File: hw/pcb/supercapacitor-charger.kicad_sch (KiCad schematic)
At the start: 13 parts, among them U2 TPS61094

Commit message: fix: updated schematics to pcb revision d
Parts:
- JP1: PN (none) -> -
- TP3: PN (none) -> -; now left out of the parts list

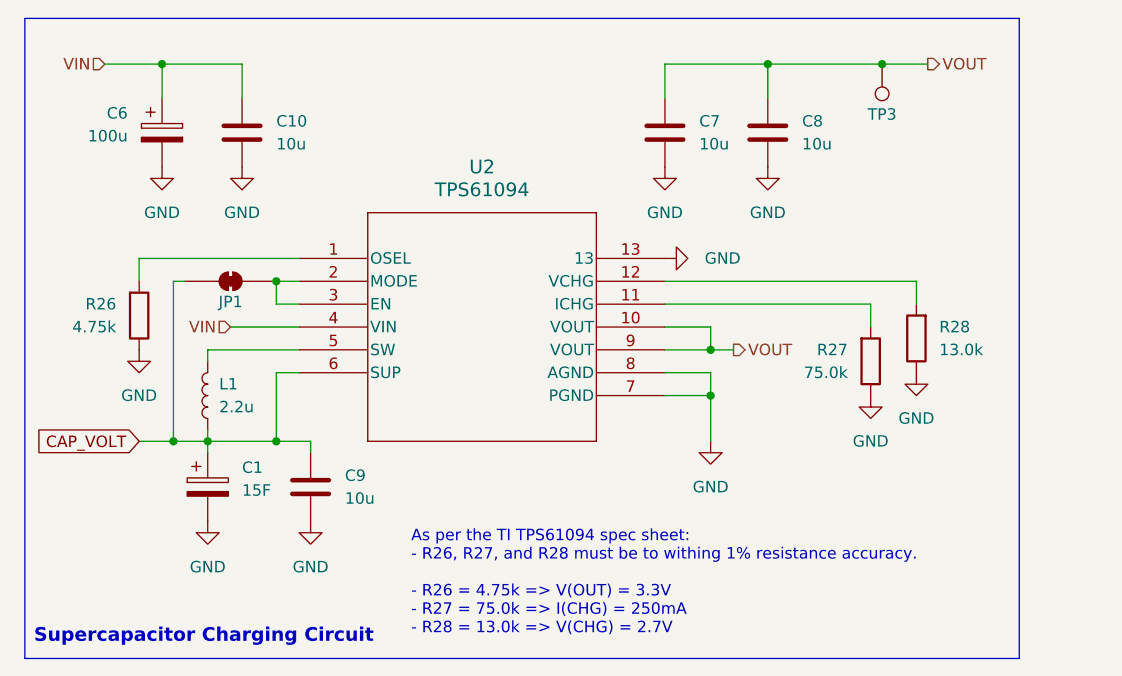
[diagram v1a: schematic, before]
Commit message: fix: added schottky diode or gate to enable pin
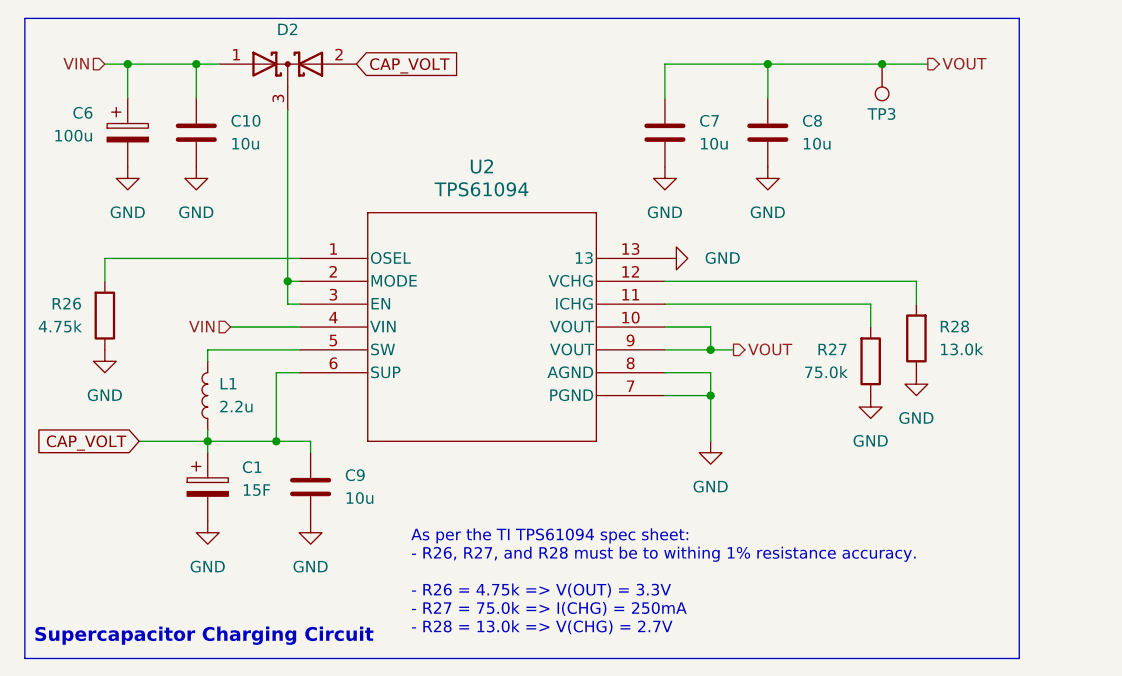
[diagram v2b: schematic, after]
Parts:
- removed JP1: SolderJumper_2_Bridged, Jumper:SolderJumper-2_P1.3mm_Bridged_RoundedPad1.0x1.5mm, symbol Jumper:SolderJumper_2_Bridged
- added D2: (no value), Package_TO_SOT_SMD:SOT-23, symbol Device:D_Schottky_Dual_CommonCathode_AAK
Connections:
- net CAP_VOLT: now also D2.2 (A)
- net VIN: now also D2.1 (A)
- net at U2.2 (MODE), U2.3 (EN): now also D2.3 (K)
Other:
- moved on the sheet: C10, C6, R26

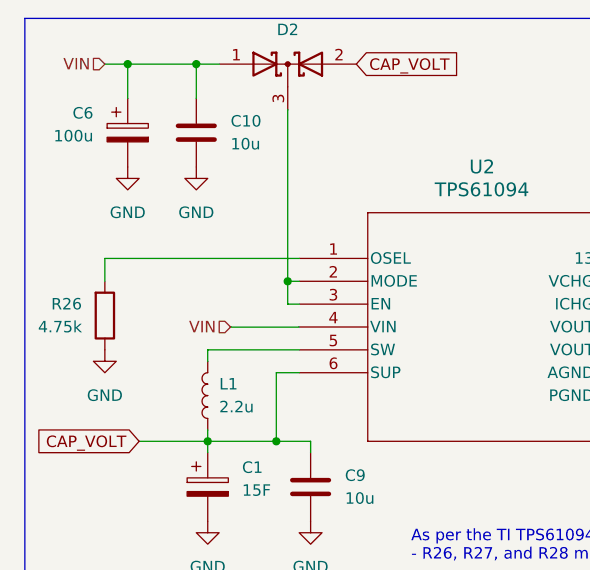
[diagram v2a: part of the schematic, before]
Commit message: fix: added or-ing diode to board
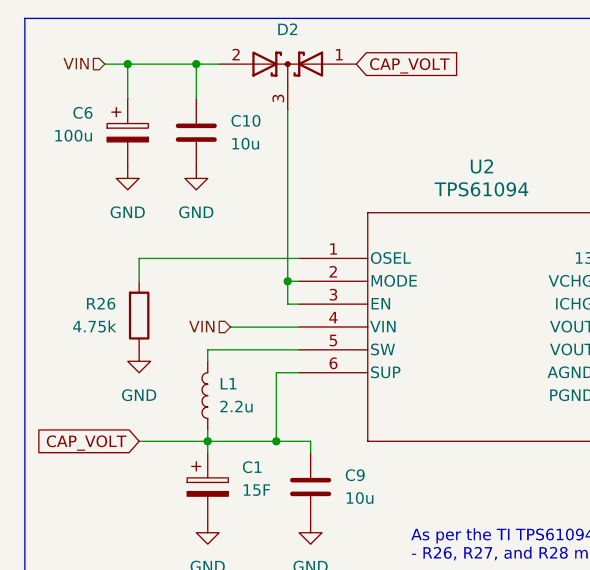
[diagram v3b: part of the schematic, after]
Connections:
- net CAP_VOLT: now also D2.1 (A); no longer D2.2 (A)
- net VIN: now also D2.2 (A); no longer D2.1 (A)
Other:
- moved on the sheet: R26
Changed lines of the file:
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@@
 	(wire
 		(pts
-			(xy 125.73 97.79) (xy 104.14 97.79)
+			(xy 125.73 97.79) (xy 107.95 97.79)
 		)
 		(stroke
@@
 	(wire
 		(pts
-			(xy 104.14 97.79) (xy 104.14 100.33)
+			(xy 107.95 97.79) (xy 107.95 100.33)
 		)
 		(stroke
@@
 	(symbol
 		(lib_id "power:GND")
-		(at 104.14 107.95 0)
+		(at 107.95 107.95 0)
 		(mirror y)
 		(unit 1)
@@
 		(fields_autoplaced yes)
 		(property "Reference" "#PWR034"
-			(at 104.14 114.3 0)
+			(at 107.95 114.3 0)
 			(hide yes)
 			(show_name no)
@@
 		)
 		(property "Value" "GND"
-			(at 104.14 113.03 0)
+			(at 107.95 113.03 0)
 			(show_name no)
 			(do_not_autoplace no)
@@
 		)
 		(property "Footprint" ""
-			(at 104.14 107.95 0)
+			(at 107.95 107.95 0)
 			(hide yes)
 			(show_name no)
@@
 		)
 		(property "Datasheet" ""
-			(at 104.14 107.95 0)
+			(at 107.95 107.95 0)
 			(hide yes)
 			(show_name no)
@@
 		)
 		(property "Description" "Power symbol creates a global label with name \"GND\" , ground"
-			(at 104.14 107.95 0)
+			(at 107.95 107.95 0)
 			(hide yes)
 			(show_name no)
@@
 	(symbol
 		(lib_id "Device:R")
-		(at 104.14 104.14 0)
+		(at 107.95 104.14 0)
 		(mirror x)
 		(unit 1)
@@
 		(fields_autoplaced yes)
 		(property "Reference" "R26"
-			(at 101.6 102.8699 0)
+			(at 105.41 102.8699 0)
 			(show_name no)
 			(do_not_autoplace no)
@@
 		)
 		(property "Value" "4.75k"
-			(at 101.6 105.4099 0)
+			(at 105.41 105.4099 0)
 			(show_name no)
 			(do_not_autoplace no)
@@
 		)
 		(property "Footprint" "Resistor_SMD:R_0603_1608Metric"
-			(at 102.362 104.14 90)
+			(at 106.172 104.14 90)
 			(hide yes)
 			(show_name no)
@@
 		)
 		(property "Datasheet" ""
-			(at 104.14 104.14 0)
+			(at 107.95 104.14 0)
 			(hide yes)
 			(show_name no)
@@
 		)
 		(property "Description" "Resistor"
-			(at 104.14 104.14 0)
+			(at 107.95 104.14 0)
 			(hide yes)
 			(show_name no)
@@
 		)
 		(property "PN" "CPF0603F4K75C1"
-			(at 104.14 104.14 0)
+			(at 107.95 104.14 0)
 			(hide yes)
 			(show_name no)
@@
 		)
 		(property "Field6" ""
-			(at 104.14 104.14 0)
+			(at 107.95 104.14 0)
 			(hide yes)
 			(show_name no)
@@
 		)
 		(property "Sim.Device" ""
-			(at 104.14 104.14 0)
+			(at 107.95 104.14 0)
 			(hide yes)
 			(show_name no)
@@
 		)
 		(property "Sim.Type" ""
-			(at 104.14 104.14 0)
+			(at 107.95 104.14 0)
 			(hide yes)
 			(show_name no)
@@
 		(lib_id "Device:D_Schottky_Dual_CommonCathode_AAK")
 		(at 124.46 76.2 0)
+		(mirror y)
 		(unit 1)
 		(body_style 1)
@@
 		(in_pos_files yes)
 		(dnp no)
-		(fields_autoplaced yes)
 		(property "Reference" "D2"
 			(at 124.46 72.39 0)

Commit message: chore: added stars to potentially different components
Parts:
- R28: value 13.0k -> 13.0k*
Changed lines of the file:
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@@
 			)
 		)
-		(property "Value" "13.0k"
+		(property "Value" "13.0k*"
 			(at 196.85 107.9499 0)
 			(show_name no)
